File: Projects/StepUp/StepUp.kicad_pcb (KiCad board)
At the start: 4 copper layers, 101 x 81 mm, 158 parts, among them J1 USB_C_Receptacle_USB2.0_16P, J10 Conn_02x03_Odd_Even, J11 Conn_01x02, J12 Conn_02x03_Odd_Even, J2 Conn_01x02, J3 Conn_02x03_Odd_Even, J4 Conn_02x06_Odd_Even, J5 TBLH10-350-04BK, J6 Conn_01x02, J7 Conn_01x02, J8 Conn_01x02, J9 Conn_01x02, Q1 BSS84, Q2 2N7002, Q3 PMF170XP,115, Q4 BSS83P, Q5 BSS83P, SW1 FSM8JSMASTR, SW2 FSM8JSMASTR, SW3 FSM8JSMASTR, U1 USBLC6-2SC6, U2 W25Q128JVS, U3 RP2040, U4 FM24CL16B, U5 TMC2300-LA, U6 LDL1117S33R, U7 MCP73832T-2ACI_OT, U8 MIC2253, Y1 ABM8-272-T3

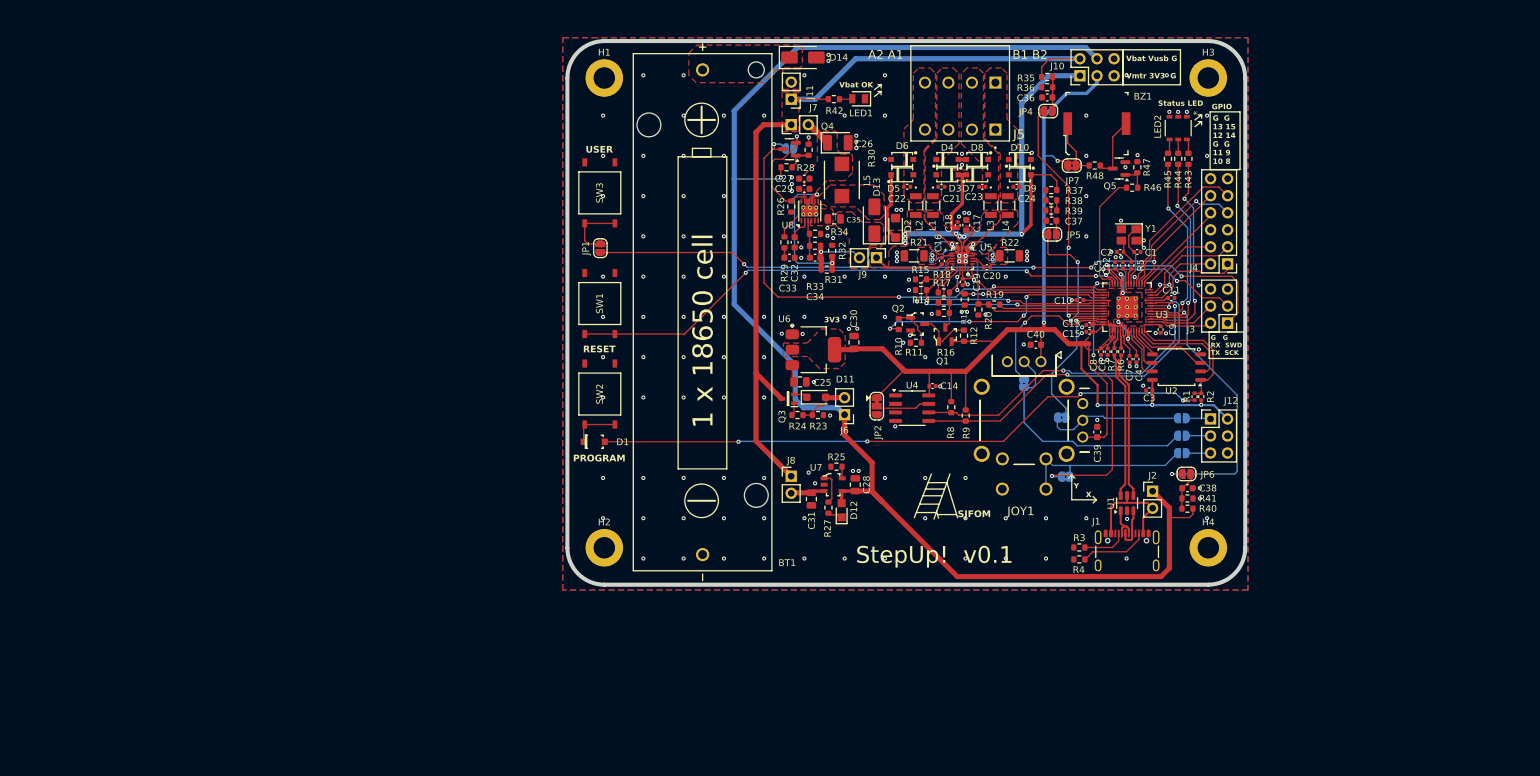
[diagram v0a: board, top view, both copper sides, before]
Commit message: feat(v0.2): Schematic updated, PCB layout start
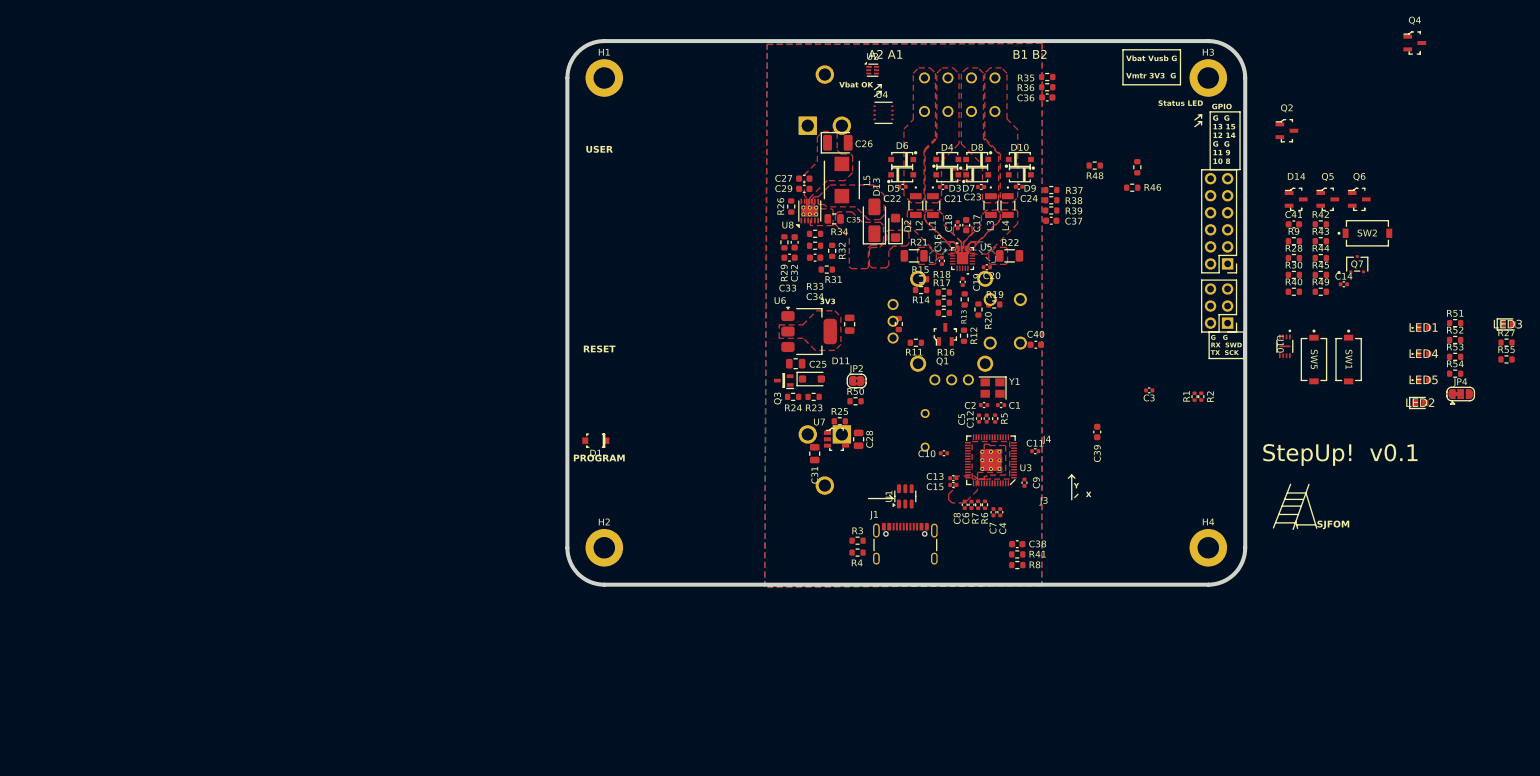
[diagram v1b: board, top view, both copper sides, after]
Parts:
- removed BT1: 1043P, Keystone:BAT_1043P
- removed D12: LTST-C170KFKT, digikey-footprints:0805
- removed J10, J12: Conn_02x03_Odd_Even, Connector_PinHeader_2.54mm:PinHeader_2x03_P2.54mm_Vertical
- removed J11, J2, J6, J7, J8, J9: Conn_01x02, Connector_PinHeader_2.54mm:PinHeader_1x02_P2.54mm_Vertical
- removed JP1, JP10, JP11, JP12, JP3, JP5, JP6: SolderJumper_2_Open, Jumper:SolderJumper-2_P1.3mm_Open_RoundedPad1.0x1.5mm
- removed JP13, JP7, JP8, JP9: SolderJumper_2_Bridged, Jumper:SolderJumper-2_P1.3mm_Bridged2Bar_RoundedPad1.0x1.5mm
- removed SW3: FSM8JSMASTR, Snapeda:SW4_FSM8JSMASTR_TEC
- added BT2: 54, Samacsys:54, B.Cu at (66.1, 82.1)
- added BT3: 54, Samacsys:54, B.Cu at (61.1, 36.1)
- added C41: 1uF, Capacitor_SMD:C_0603_1608Metric, F.Cu at (133.5, 50.8)
- added LED3: 150060AS75000, Samacsys:LEDC1608X80N, F.Cu at (165.4, 65.7)
- added LED4: IN-S63AT5UW, Samacsys:INS63AT5UW, F.Cu at (152.8, 70.1)
- added LED5: IN-S63AT5UW, Samacsys:INS63AT5UW, F.Cu at (152.8, 74.0)
- added Q6: 2N7002-7-F, digikey-footprints:SOT-23-3, F.Cu at (143.2, 47.1)
- added Q7: SSM3J328R_LF, Snapeda:SOT-23F_TOS, F.Cu at (142.9, 56.8)
- added R49: 100R, Resistor_SMD:R_0603_1608Metric, F.Cu at (137.5, 60.9)
- added R50: 0R, Resistor_SMD:R_0603_1608Metric, F.Cu at (68.2, 77.2)
- added R51: 124R, Resistor_SMD:R_0603_1608Metric, F.Cu at (157.5, 65.5)
- added R52: 261R, Resistor_SMD:R_0603_1608Metric, F.Cu at (157.5, 68.0)
- added R53: 124R, Resistor_SMD:R_0603_1608Metric, F.Cu at (157.5, 70.6)
- added R54: 124R, Resistor_SMD:R_0603_1608Metric, F.Cu at (157.5, 73.1)
- added R55: 0R, Resistor_SMD:R_0603_1608Metric, F.Cu at (165.2, 71.0)
- added SW5: PTS636SL43SMTRLFS, Snapeda:SW_PTS636S-J_CNK, F.Cu at (136.5, 71.0)
- added U10: W25Q16JVUXIQ TR, Snapeda:USON-8_UX_2x3x0p6_WIN, F.Cu at (132.1, 69.0)
- BZ1: value PKMCS0909E4000-R1 -> PS1240P02CT3; footprint digikey-footprints:Piezo_9x9mm_PKMCS0909E4000-R1 -> Samacsys:PS1240P02BT; moved to B.Cu
- D14: value SK54A-LTP -> BAT54C-7-F; footprint Diode_SMD:D_SMA -> digikey-footprints:SOT-23-3
- J5: value TBLH10-350-04BK -> 1862068; footprint Snapeda:CUI_TBLH10-350-04BK -> Snapeda:1862068_PHOENIX_1862068; moved to B.Cu
- JOY1: moved to B.Cu
- JP2: value SolderJumper_3_Open -> SolderJumper_2_Bridged; footprint Jumper:SolderJumper-3_P1.3mm_Bridged12_RoundedPad1.0x1.5mm -> Jumper:SolderJumper-2_P1.3mm_Bridged2Bar_RoundedPad1.0x1.5mm
- JP4: value SolderJumper_2_Open -> SolderJumper_3_Bridged12; footprint Jumper:SolderJumper-2_P1.3mm_Open_RoundedPad1.0x1.5mm -> Jumper:SolderJumper-3_P1.3mm_Bridged12_RoundedPad1.0x1.5mm
- LED1: value LTST-C171GKT -> IN-S63AT5UW; footprint Samacsys:LEDC2012X90N -> Samacsys:INS63AT5UW
- LED2: value APF3236LSEEZGKQBKC -> 150060RS75000; footprint Snapeda:APF3236LSEEZGKQBKC_KNB -> Samacsys:LEDC1608X80N
- Q2: value 2N7002 -> 2N7002-7-F
- Q4, Q5: value BSS83P -> 2N7002-7-F; footprint Package_TO_SOT_SMD:SOT-23 -> digikey-footprints:SOT-23-3
- R25: value 2kR -> 2.7kR
- R28: value 100R -> 0R
- R30, R40: value 100kR -> 5.1MR
- R42: value 620R -> 100R
- R43: value 750R -> 330R
- R44: value 330R -> 1Meg
- R45: value 330R -> 100kR
- R8: value 10kR -> 56kR
- R9: value 10kR -> 2.2kR
- SW1, SW2: value FSM8JSMASTR -> PTS636SL43SMTRLFS; footprint Snapeda:SW4_FSM8JSMASTR_TEC -> Snapeda:SW_PTS636S-J_CNK
- U2: value W25Q128JVS -> BQ297xy; footprint Package_SO:SOIC-8_5.23x5.23mm_P1.27mm -> Package_SON:WSON-6_1.5x1.5mm_P0.5mm
- U4: value FM24CL16B -> ECH8697R-TL-W; footprint Package_SO:SOIC-8_3.9x4.9mm_P1.27mm -> Snapeda:SOT-28FL-8_2P9X2P3_ONS
- moved SW2 116.9 mm to (144.4, 52.1), turned to 0 degrees
- moved SW1 111.9 mm to (141.7, 71.0), turned to -90 degrees
- moved R27 104.0 mm to (165.2, 68.4), turned to 0 degrees
- moved Q4 94.5 mm to (151.5, 23.8), turned to 0 degrees
- moved LED1 90.8 mm to (152.8, 66.2), turned to 0 degrees
- moved R28 76.8 mm to (133.5, 55.8)
- moved D14 76.5 mm to (133.8, 47.1)
- moved R42 74.9 mm to (137.5, 50.8), turned to 0 degrees
- moved R30 74.7 mm to (133.5, 58.4), turned to 0 degrees
- moved JP4 74.5 mm to (158.3, 76.1), turned to 0 degrees
- moved U2 63.3 mm to (70.7, 27.9), turned to 0 degrees
- moved C14 63.1 mm to (140.9, 59.8)
- moved Q2 62.1 mm to (132.4, 36.9)
- moved R9 55.4 mm to (133.5, 53.3), turned to 0 degrees
- moved LED2 54.6 mm to (152.3, 77.4), turned to 0 degrees
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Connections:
- BZ1 pad 1: Net-(JP7-A) -> (no net)
- BZ1 pad 2: Net-(Q5-D) -> Net-(JP4-C)
- C14 pad 1: +3V3 -> Net-(U2-BAT)
- C14 pad 2: GND -> /Power/VBAT_PACK_NEG
- C31 pad 1: Net-(J8-Pin_2) -> Vbat
- C36 pad 2: Net-(JP4-A) -> VBAT_MONITOR
- C37 pad 2: Net-(JP5-A) -> VMOTOR_MONITOR
- C38 pad 2: Net-(JP6-A) -> VUSB_MONITOR
- D14 pad 1: Net-(D14-K) -> Net-(Q6-D)
- D14 pad 2: GND -> MCU_PWR_BTN
- J1 pad A4: Net-(J2-Pin_2) -> V_USB
- J1 pad A9: Net-(J2-Pin_2) -> V_USB
- J1 pad B4: Net-(J2-Pin_2) -> V_USB
- J1 pad B9: Net-(J2-Pin_2) -> V_USB
- J4 pad 1: /MCU/GPIO8 -> unconnected-(J4-Pin_1-Pad1)
- JOY1 pad 11: +3V3 -> GND
- JOY1 pad 12: /User Input/JOYSTICK_AXIS_V -> JOY_AXIS_MCU_V
- JOY1 pad 13: GND -> +3V3
- JOY1 pad 2: /User Input/JOYSTICK_AXIS_H -> JOY_AXIS_MCU_H
- JOY1 pad A1: GND -> JOY_MCU_BTN
- JOY1 pad B1: /User Input/JOYSTICK_BUTTON -> JOY_MCU_BTN
- JOY1 pad D1: /User Input/JOYSTICK_BUTTON -> GND
- JP2 pad 1: +3V3 -> Net-(D11-A)
- JP2 pad 2: Net-(JP2-C) -> V_USB
- JP4 pad 1: Net-(JP4-A) -> +3V3
- JP4 pad 2: VBAT_MONITOR -> Net-(JP4-C)
- LED2 pad 2: GND -> Net-(LED2-A)
- Q4 pad 2: /Power/BOOST_ENABLE -> GND
- Q4 pad 3: MCU_BOOST_EN -> Net-(Q4-D)
- Q5 pad 1: Net-(Q5-G) -> /Power/VBAT_PACK_NEG
- R26 pad 2: /Power/BOOST_ENABLE -> MCU_BOOST_EN
- R28 pad 1: V_USB -> Net-(U4-S1)
- R28 pad 2: Net-(Q4-G) -> /Power/VBAT_PACK_NEG
- R30 pad 1: GND -> Net-(U2-Dout)
- R30 pad 2: Net-(Q4-G) -> /Power/VBAT_PACK_NEG
- R35 pad 1: Net-(JP4-A) -> VBAT_MONITOR
- R36 pad 2: Net-(JP4-A) -> VBAT_MONITOR
- R37 pad 1: Net-(JP5-A) -> VMOTOR_MONITOR
- R38 pad 1: Net-(JP5-A) -> VMOTOR_MONITOR
- R40 pad 1: Net-(JP6-A) -> GND
- R40 pad 2: V_USB -> Net-(U2-Cout)
- R41 pad 2: Net-(JP6-A) -> VUSB_MONITOR
- R42 pad 1: Net-(LED1-A) -> Net-(Q5-D)
- R42 pad 2: Vbat -> Net-(U2-Cout)
- R43 pad 1: LED_RED -> Net-(U2-BAT)
- R43 pad 2: Net-(LED2-Pad4) -> /Power/VBAT_PACK_POS
- R44 pad 1: LED_GREEN -> Net-(Q6-D)
- R44 pad 2: Net-(LED2-Pad5) -> /Power/VBAT_PACK_POS
- R45 pad 1: LED_BLUE -> +3V3
- R45 pad 2: Net-(LED2-Pad6) -> MCU_PWR_CTRL
- R46 pad 2: Net-(Q5-G) -> Net-(Q4-G)
- R47 pad 2: Net-(Q5-G) -> Net-(Q4-G)
- R48 pad 1: Net-(Q5-D) -> Net-(Q4-D)
- R48 pad 2: Net-(JP7-A) -> Net-(JP4-C)
- R8 pad 1: /MCU/EEPROM_SCL -> VUSB_MONITOR
- R8 pad 2: +3V3 -> V_USB
- R9 pad 1: /MCU/EEPROM_SDA -> GND
- R9 pad 2: +3V3 -> Net-(U2-V-)
- SW1 pad 1: /MCU/RUN -> GND
- SW1 pad 2: /MCU/RUN -> Net-(D1-PadK)
- SW2 pad 1: Net-(D1-PadK) -> GND
- SW2 pad 2: Net-(D1-PadK) -> Net-(D14-Pad3)
- U1 pad 5: Net-(J2-Pin_2) -> V_USB
- U2 pad 1: /MCU/QSPI_SS -> unconnected-(U2-NC-Pad1)
- U2 pad 2: /MCU/QSPI_SD1 -> Net-(U2-Cout)
- U2 pad 3: /MCU/QSPI_SD2 -> Net-(U2-Dout)
- U2 pad 4: GND -> /Power/VBAT_PACK_NEG
- U2 pad 5: /MCU/QSPI_SD0 -> Net-(U2-BAT)
- U2 pad 6: /MCU/QSPI_SCLK -> Net-(U2-V-)
- U3 pad 11: /MCU/GPIO8 -> MCU_PWR_BTN
- U3 pad 4: LED_RED -> MCU_LED_ERROR
- U3 pad 5: LED_GREEN -> MCU_LED_STATUS_1
- U3 pad 7: LED_BLUE -> MCU_LED_STATUS_2
- U3 pad 8: /MCU/EEPROM_SDA -> MCU_LED_STATUS_3
- U3 pad 9: /MCU/EEPROM_SCL -> MCU_PWR_CTRL
- U4 pad 1: unconnected-(U4-Pad1) -> Net-(U4-S1)
- U4 pad 2: unconnected-(U4-Pad2) -> Net-(U2-Dout)
- U4 pad 3: unconnected-(U4-Pad3) -> GND
- U4 pad 4: GND -> Net-(U2-Cout)
- U4 pad 5: /MCU/EEPROM_SDA -> Net-(U4-D-Pad5)
- U4 pad 6: /MCU/EEPROM_SCL -> Net-(U4-D-Pad5)
- U4 pad 7: Net-(JP2-C) -> Net-(U4-D-Pad5)
- U4 pad 8: +3V3 -> Net-(U4-D-Pad5)
- U7 pad 3: Net-(J8-Pin_2) -> Vbat
- U8 pad 11: /Power/BOOST_ENABLE -> MCU_BOOST_EN
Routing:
- net V_USB: track 211.0 -> 0.00 mm, vias 1 -> 0
- net +3V3: track 206.4 -> 0.00 mm, vias 5 -> 0
- net Vbat: track 123.3 -> 0.00 mm
- net /MCU/GPIO13: track 101.5 -> 0.00 mm, vias 4 -> 0
- net VMotor: track 96.0 -> 0.00 mm, vias 7 -> 0
- net /MCU/~{USB_BOOT}: track 91.4 -> 0.00 mm, vias 4 -> 0
- net /MCU/RUN: track 84.1 -> 0.00 mm, vias 4 -> 0
- net MCU_BOOST_EN: track 77.2 -> 0.00 mm, vias 3 -> 0
- net /MCU/EEPROM_SDA: track 53.3 -> 0.00 mm, vias 2 -> 0
- net /MCU/EEPROM_SCL: track 50.9 -> 0.00 mm, vias 2 -> 0
- net VUSB_MONITOR: track 43.8 -> 0.00 mm, vias 2 -> 0
- net JOY_MCU_BTN: track 42.1 -> 0.00 mm, vias 3 -> 0
- net VBAT_MONITOR: track 38.2 -> 0.00 mm, vias 2 -> 0
- net TMC_DIR: track 38.1 -> 0.00 mm, vias 2 -> 0
- net ~{TMC_STBDY}: track 36.9 -> 0.00 mm, vias 4 -> 0
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- removed copper zone on F.Cu, net Net-(D14-K)
- removed copper zone on F.Cu, net Vbat

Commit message: feat(v0.2): Rough layout begins
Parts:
- removed J4: Conn_02x06_Odd_Even, Connector_PinHeader_2.54mm:PinHeader_2x06_P2.54mm_Vertical
- removed the R53 at (157.5, 70.6)
- removed the R54 at (157.5, 73.1)
- removed SW5: PTS636SL43SMTRLFS, Snapeda:SW_PTS636S-J_CNK
- added R50: 100R, Resistor_SMD:R_0603_1608Metric, F.Cu at (100.3, 91.3)
- added R52: 100R, Resistor_SMD:R_0603_1608Metric, F.Cu at (100.3, 103.5)
- added SW3: 1825027-8, Samacsys:1825027-8, B.Cu at (107.8, 82.4)
- H1, H2, H3, H4: footprint MountingHole:MountingHole_3.2mm_M3_DIN965_Pad -> MountingHole:MountingHole_2.2mm_M2
- JP2: renamed from JP4; moved to B.Cu
- LED1: value IN-S63AT5UW -> IN-S63AS5A; footprint Samacsys:INS63AT5UW -> Samacsys:INS63AS5UW
- LED2: value 150060RS75000 -> IN-S63ASR; footprint Samacsys:LEDC1608X80N -> Samacsys:LEDC1706X110N
- LED3: value 150060AS75000 -> IN-S63AS5UW; footprint Samacsys:LEDC1608X80N -> Samacsys:INS63AS5UW
- LED4, LED5: value IN-S63AT5UW -> IN-S63AS5UW; footprint Samacsys:INS63AT5UW -> Samacsys:INS63AS5UW
- R49: renamed from R52; value 261R -> 220R
- R51: value 124R -> 100R
- moved H3 115.4 mm to (59.7, 126.9)
- moved R26 113.4 mm to (61.0, 113.3)
- moved Q7 107.9 mm to (82.0, 106.3), turned to -90 degrees
- moved SW2 103.9 mm to (71.1, 125.7), turned to 90 degrees
- moved R32 93.9 mm to (72.0, 82.4)
- moved SW1 93.4 mm to (65.9, 125.7), turned to 90 degrees
- moved LED1 88.7 mm to (90.1, 128.9), turned to 180 degrees
- moved JP2 86.1 mm to (77.4, 105.4), turned to 180 degrees
- moved H2 83.5 mm to (100.5, 53.1)
- moved Q2 75.8 mm to (79.9, 91.5)
- moved R55 70.9 mm to (81.2, 109.3)
- moved R53 68.6 mm to (84.3, 109.2), turned to 180 degrees
- moved LED3 68.5 mm to (101.8, 91.2), turned to -90 degrees
- moved R47 67.5 mm to (70.2, 56.9), turned to -90 degrees
- moved R54 67.3 mm to (82.1, 103.5), turned to 0 degrees
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- renumbered BT3 to BT1, C15 to C14, C16 to C15, C17 to C16, C18 to C17, C19 to C18, C20 to C19, C21 to C20, C22 to C21, C23 to C22, C24 to C23, C25 to C24, C26 to C25, C28 to C26, C29 to C28, C30 to C29, C31 to C30, C32 to C31, C33 to C32, C34 to C33, C35 to C34, C41 to C35, C14 to C36, C36 to C37, C37 to C38, C38 to C39, C39 to C40, C40 to C41, D13 to D12, D14 to D13, J3 to J2, J5 to J3, JP2 to JP1, Q6 to Q4, Q7 to Q5, Q5 to Q6, Q4 to Q7, R12 to R10, R13 to R11, R14 to R12, R15 to R13, R16 to R14, R17 to R15, R18 to R16, R19 to R17, R20 to R18, R21 to R19, R22 to R20, R23 to R21, R24 to R22, R50 to R23, R25 to R24, R26 to R25, R27 to R26, R29 to R27, R31 to R28, R32 to R29, R33 to R30, R34 to R31, R55 to R32, R44 to R33, R49 to R34, R45 to R35, R43 to R36, R28 to R37, R30 to R38, R35 to R39, R36 to R40, R37 to R41, R38 to R42, R39 to R43, R8 to R44, R41 to R45, R9 to R46, R42 to R47, R40 to R48, R46 to R53, R47 to R54, R48 to R55, R10 to R8, R11 to R9, U10 to U1, U1 to U2, U5 to U4, U6 to U5, U7 to U6, U8 to U7, U4 to U8, U2 to U9
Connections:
- BZ1 pad 1: (no net) -> Net-(Q7-D)
- D13 pad 3: Net-(D14-Pad3) -> Net-(D13-Pad3)
- LED1 pad 1: GND -> Net-(LED1-K)
- LED1 pad 2: Net-(LED1-A) -> V_USB
- LED3 pad 1: Net-(LED3-K) -> GND
- LED3 pad 2: V_USB -> Net-(LED3-A)
- Q7 pad 3: Net-(Q4-D) (its old number) -> Net-(Q7-D)
- R26 pad 2: Net-(LED3-K) -> Net-(LED1-K)
- R51 pad 1: MCU_LED_STATUS_1 -> Net-(LED4-A)
- R51 pad 2: Net-(LED1-A) -> MCU_LED_STATUS_2
- R55 pad 1: Net-(Q4-D) (its old number) -> Net-(Q7-D)
- SW1 pad 2: Net-(D1-PadK) -> /MCU/RUN
- SW2 pad 2: Net-(D14-Pad3) -> Net-(D1-PadK)
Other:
- board size 101 x 81 mm -> 47 x 81 mm
- board text added: "47.0223 mm x 81.0223 mm"
- board text added: "A1 A2"
- board text added: "B2 B1"
- board text added: "BottomLayer_Mask.Mask"
- board text added: "BottomLayer_Paste.Paste"
- board text added: "BottomLayer_Silk.Silkscreen"
- board text added: "L1_TopLayer.Cu"
- board text added: "L2_InnerLayer1.Cu"
- board text added: "L3_InnerLayer1.Cu"
- board text added: "L4_BottomLayer.Cu"
- board text added: "POWER"
- board text added: "StepUp! v0.2"
- board text added: "TopLayer_Mask.Mask"
- board text added: "TopLayer_Paste.Paste"
- board text added: "TopLayer_Silk.Silkscreen"
- board text removed: "101.0000 mm x 81.0000 mm"
- board text removed: "A2 A1"
- board text removed: "B.Cu"
- board text removed: "B.Mask"
- board text removed: "B.Paste"
- board text removed: "B.Silkscreen"
- board text removed: "B1 B2"
- board text removed: "F.Cu"
- board text removed: "F.Mask"
- board text removed: "F.Paste"
- board text removed: "F.Silkscreen"
- board text removed: "G G 13 15 12 14 G G 11 9 10 8"
- board text removed: "GPIO"
- board text removed: "In1.Cu"
- board text removed: "In2.Cu"
- board text removed: "Status LED"
- board text removed: "StepUp! v0.1"
- board text removed: "USER"
- board text removed: "Vbat Vusb G Vmtr 3V3 G"
- board text removed: "X"
- board text removed: "Y"

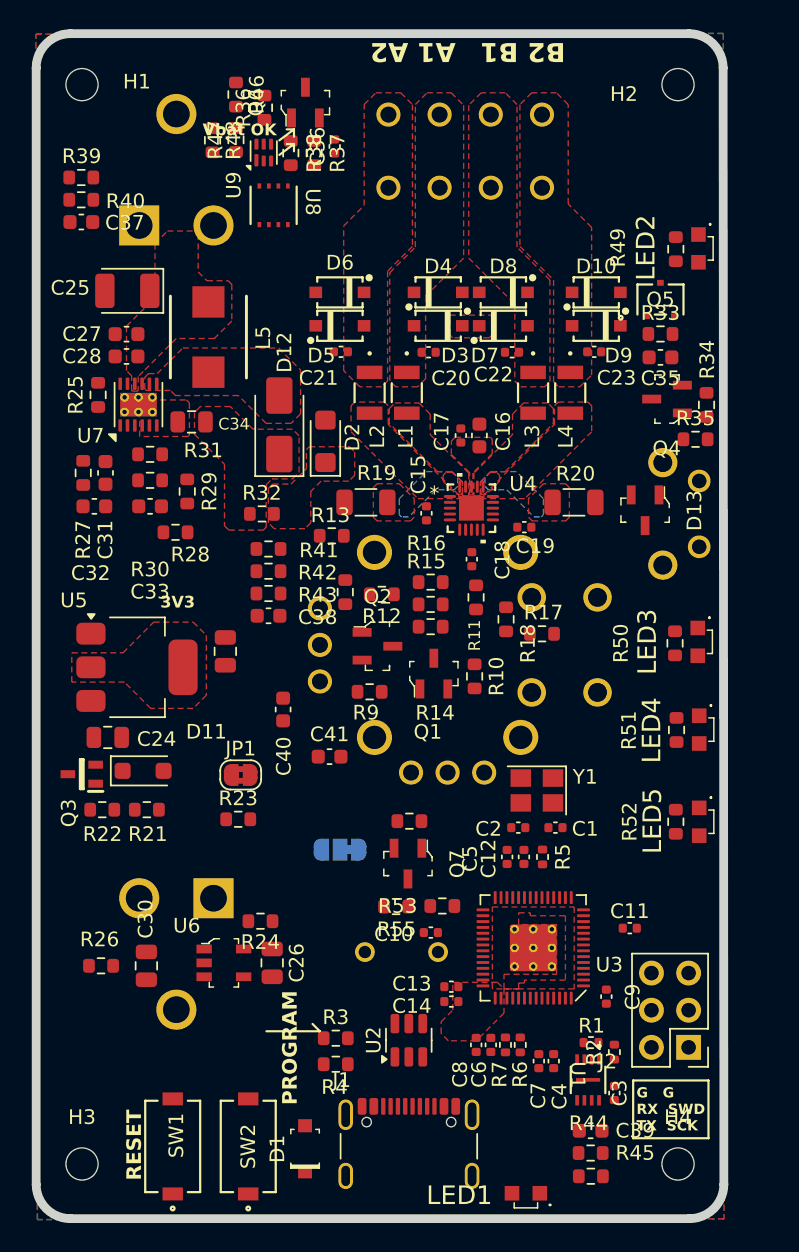
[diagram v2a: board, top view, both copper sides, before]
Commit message: feat(cad): CAD dims pushed to PCB
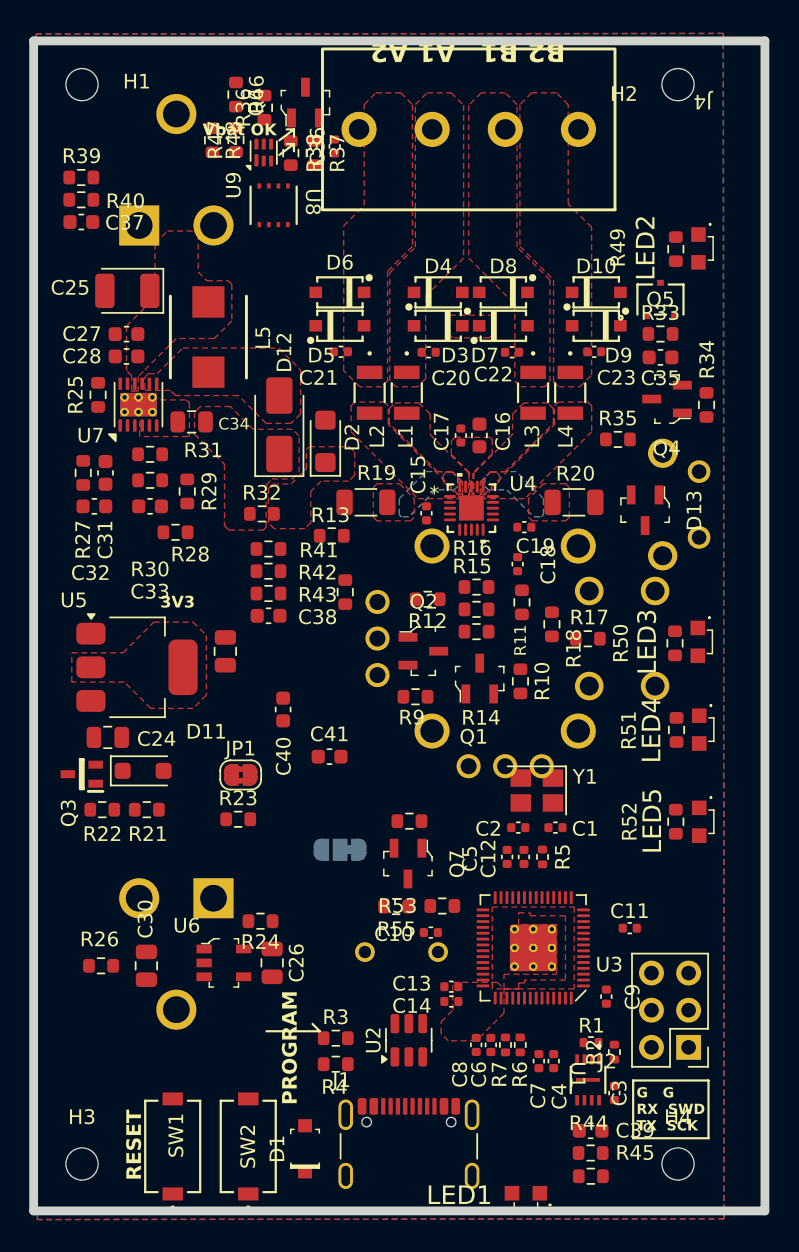
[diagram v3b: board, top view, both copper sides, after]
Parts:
- removed J3: 1862068, Snapeda:1862068_PHOENIX_1862068
- added J4: AST250404, my_parts:AST250404, F.Cu at (93.7, 56.1)
- moved R35 5.31 mm to (96.3, 77.3)
- moved JOY1 3.96 mm to (79.9, 93.5)
- moved Q1 3.15 mm to (86.9, 93.7)
- moved Q2 3.15 mm to (83.0, 91.8)
- moved R10 3.15 mm to (89.7, 93.9)
- moved R11 3.15 mm to (89.8, 88.5)
- moved R12 3.15 mm to (83.3, 88.3)
- moved R14 3.15 mm to (86.7, 90.5)
- moved R15 3.15 mm to (86.7, 89.0)
- moved R16 3.15 mm to (86.7, 87.4)
- moved R17 3.15 mm to (94.3, 91.0)
- moved R18 3.15 mm to (91.8, 90.0)
- moved R9 3.15 mm to (82.5, 94.9)
- moved C18 3.15 mm to (89.5, 85.9)
- moved SW3 0.64 mm to (107.8, 81.8)
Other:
- board size 47 x 81 mm -> 50 x 80 mm
